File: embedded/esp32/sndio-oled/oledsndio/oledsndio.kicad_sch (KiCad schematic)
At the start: 30 parts

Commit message: Schematic Done
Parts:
- added C10: 10u, symbol Device:C_Small
- added C11: 100n, symbol Device:C_Small
- added U6: INMP441_MODULE, symbol inmp441:INMP441_MODULE
- gave numbers to parts that had none: 30
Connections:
- net +3V3: now also C10.1, C11.1, U6.2 (VDD)
- net GND: now also C10.2, C11.2, U6.3 (GND), U6.4 (LRC)
- net MIC_SCK: now also U6.6 (SCK)
- net MIC_CS renamed MIC_WS
- net MIC_WS: now also U6.5 (WS)
- net MIC_MISO renamed MIC_SD
- net MIC_SD: now also U6.1 (SD)
- net MIC_MOSI: no longer names the net of U1.37 (IO23)
- no-connect marks 26 -> 27
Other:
- note added: "MEMS MICROPHONE"

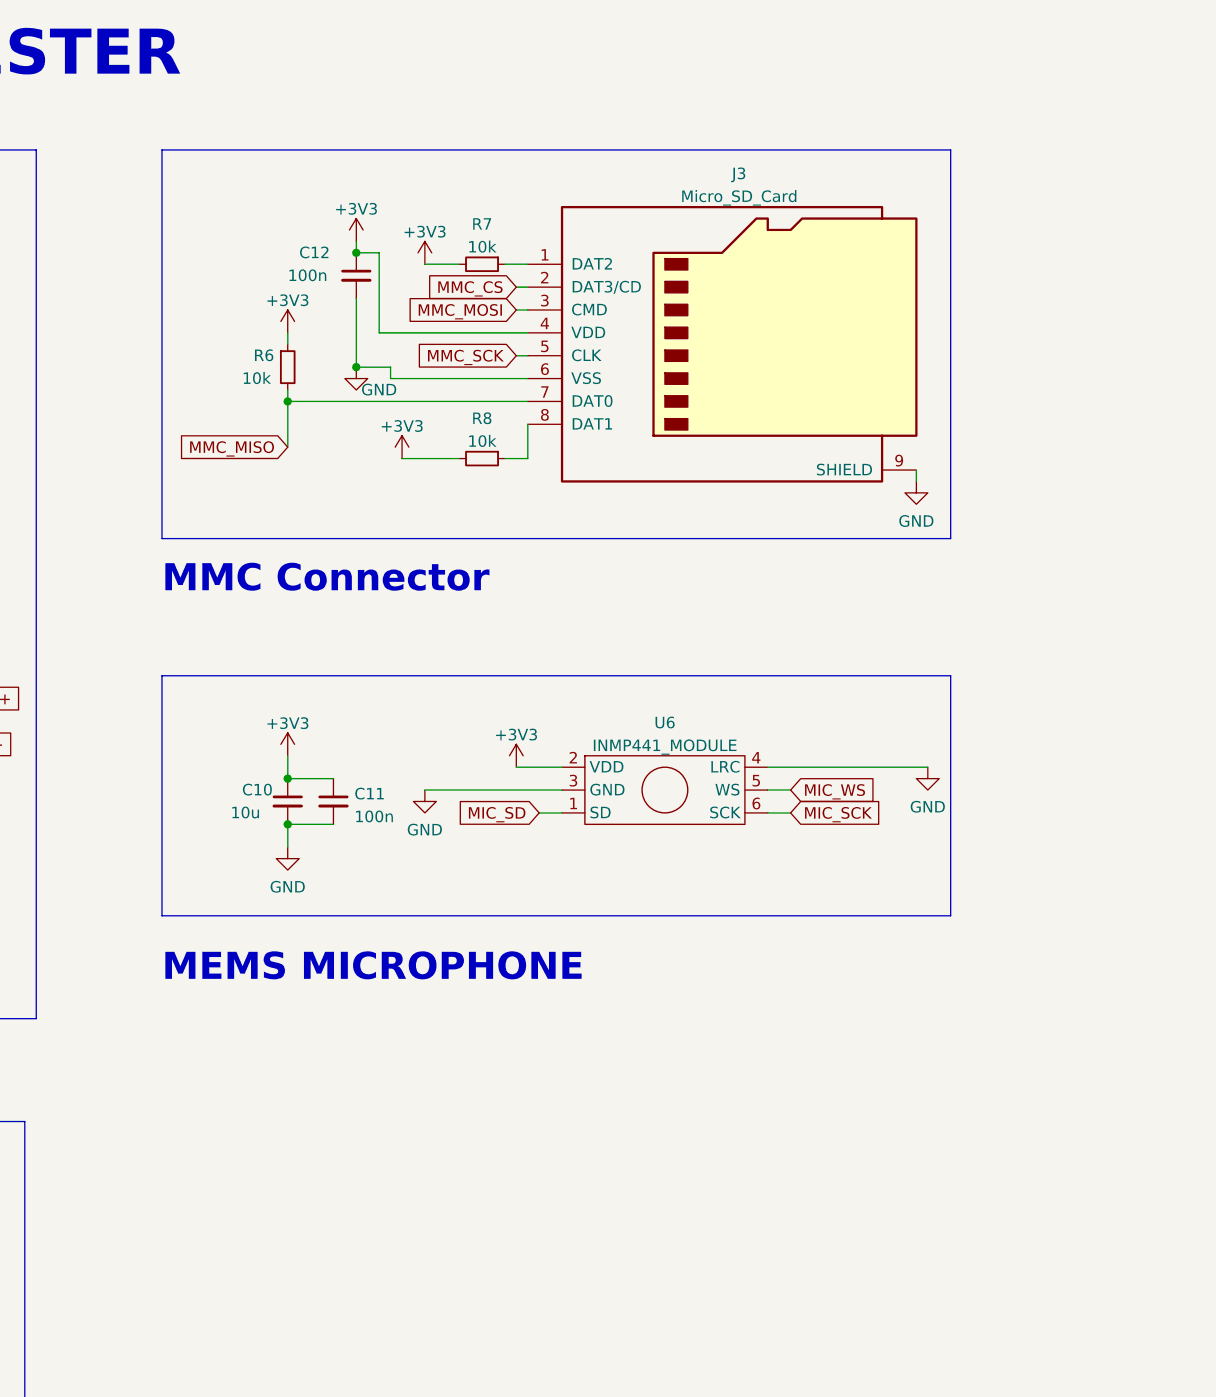
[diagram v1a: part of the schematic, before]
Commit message: ESP32 Audio
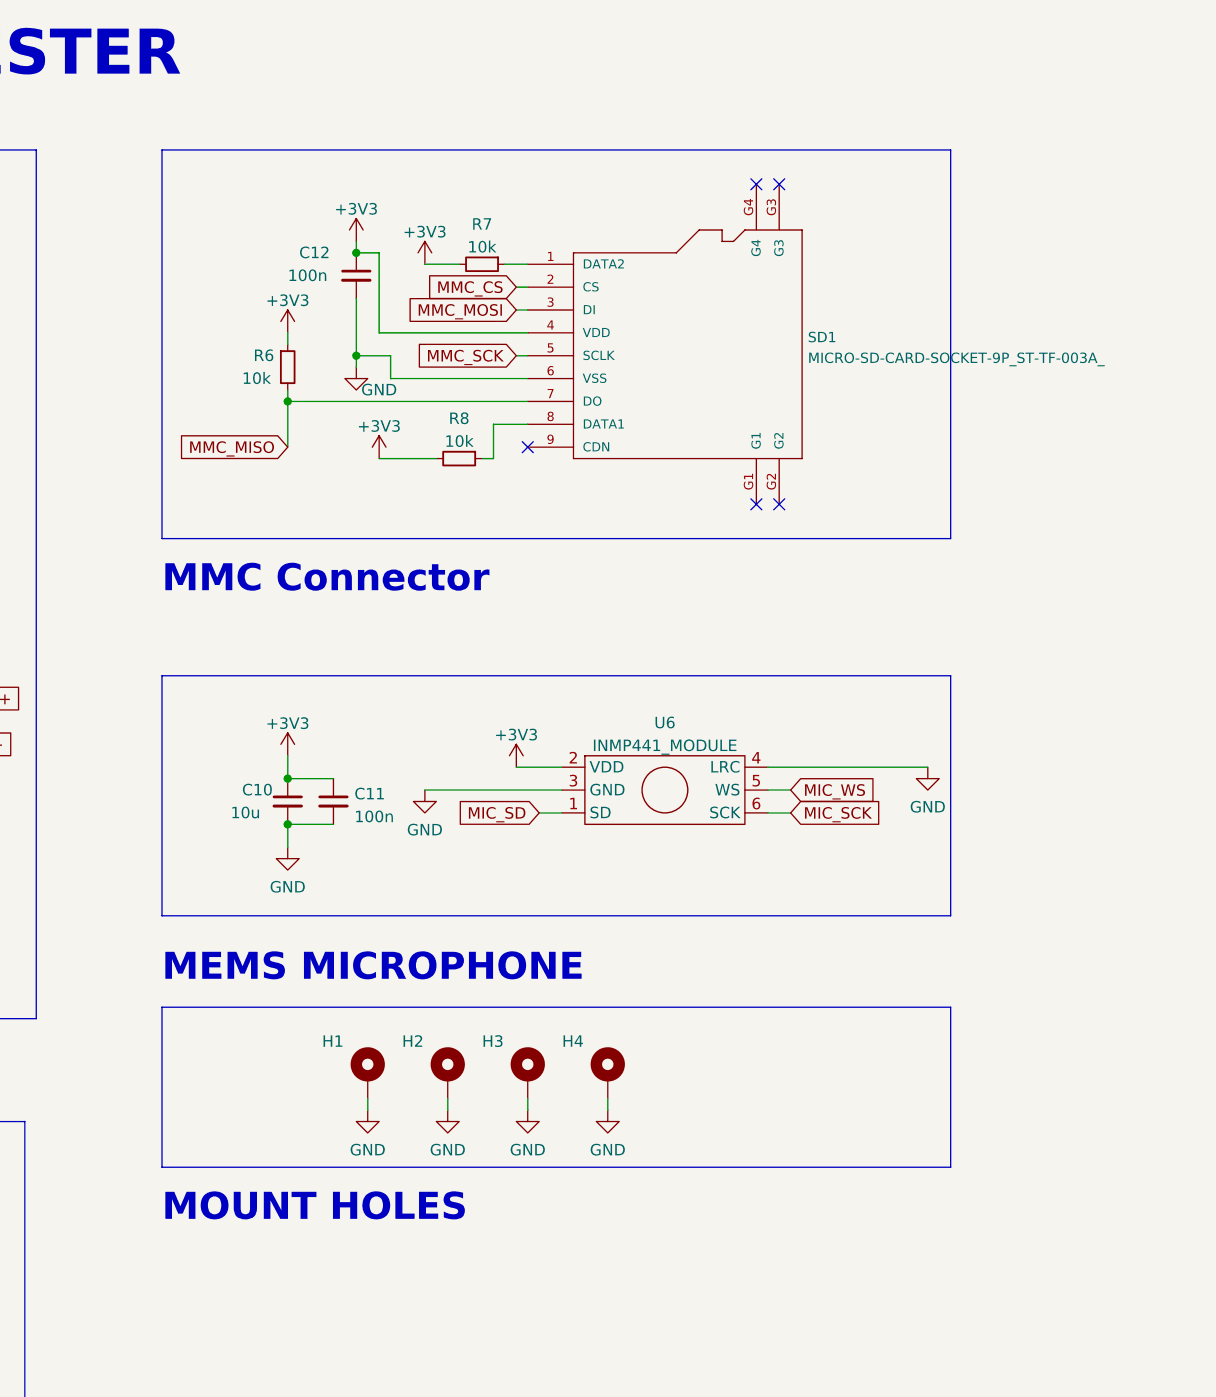
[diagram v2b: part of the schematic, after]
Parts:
- removed J3: Micro_SD_Card, symbol Connector:Micro_SD_Card
- added H1, H2, H3, H4: MountingHole_Pad, MountingHole:MountingHole_5.3mm_M5_Pad, symbol Mechanical:MountingHole_Pad
- added SD1: MICRO-SD-CARD-SOCKET-9P_ST-TF-003A_, OPL_Connector:MICRO-SD9+4P-SMD-16.1X14.5X1.85MM, symbol OPL_Connector:MICRO-SD-CARD-SOCKET-9P_ST-TF-003A_
- C1, C10, C11, C12, C2, C3, C4, C5, C6, C7, C8, C9: footprint (none) -> Capacitor_SMD:C_0805_2012Metric_Pad1.18x1.45mm_HandSolder
- D1: footprint (none) -> LED_SMD:LED_0805_2012Metric_Pad1.15x1.40mm_HandSolder
- J1: footprint (none) -> Connector_PinHeader_2.54mm:PinHeader_1x04_P2.54mm_Vertical
- J2: footprint (none) -> Connector_USB:USB_Micro-B_Wuerth_629105150521
- R1, R2, R3, R4, R5, R6, R7, R8: footprint (none) -> Resistor_SMD:R_0805_2012Metric_Pad1.20x1.40mm_HandSolder
- SW1, SW2: footprint (none) -> Button_Switch_THT:SW_PUSH_6mm
- U2: footprint (none) -> SSD1306:Display_128x64_096_I2C
- U6: footprint (none) -> INMP441:INMP441
- Y1: footprint (none) -> Crystal:Crystal_SMD_HC49-SD_HandSoldering
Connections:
- net +3V3: now also SD1.4 (VDD)
- net GND: now also H1.1, H2.1, H3.1, H4.1, SD1.6 (VSS)
- net MMC_CS: now also SD1.2 (CS)
- net MMC_MISO: now also SD1.7 (DO)
- net MMC_MOSI: now also SD1.3 (DI)
- net MMC_SCK: now also SD1.5 (SCLK)
- net at R7.1: now also SD1.1 (DATA2)
- net at R8.1: now also SD1.8 (DATA1)
- no-connect marks 27 -> 32
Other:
- note added: "MOUNT HOLES"
- moved on the sheet: R8
